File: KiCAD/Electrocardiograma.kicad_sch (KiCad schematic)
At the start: 48 parts, among them J2 Conn_01x02_Pin, J3 AudioJack4, SW1 SW_DPST_x2, U1 INA823DT, U2 ESP32-C3-WROOM-02, U4 TLV4888, U5 TLV4888

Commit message: Es raro mandar cada cambio por si acaso tu lo quieres ver
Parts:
- added U3: AMS1117-3.3, Package_TO_SOT_SMD:SOT-223-3_TabPin2, symbol Regulator_Linear:AMS1117-3.3
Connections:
- net +BATT: now also U3.3 (VI)
- net -BATT: now also U2.19 (GND), U2.9 (GND), U3.1 (GND)
- net +3.3V: now reaches U2.1 (3V3)
- net +3.3V: now also U2.2 (EN), U3.2 (VO)
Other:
- moved on the sheet: U2

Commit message: footprints resistencias
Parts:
- R1, R10, R11, R12, R13, R14, R15, R16, R17, R18, R19, R2, R20, R21, R22, R23, R24, R25, R26, R27, R3, R4, R5, R6, R7, R8, R9: footprint (none) -> Resistor_SMD:R_0805_2012Metric
- SW1: footprint (none) -> Button_Switch_THT:SW_Push_2P1T_Toggle_CK_PVA1xxH1xxxxxxV2
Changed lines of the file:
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@@
 			)
 		)
-		(property "Footprint" ""
+		(property "Footprint" "Resistor_SMD:R_0805_2012Metric"
 			(at 130.81 97.028 90)
 			(hide yes)
@@
 			)
 		)
-		(property "Footprint" ""
+		(property "Footprint" "Resistor_SMD:R_0805_2012Metric"
 			(at 80.01 165.608 90)
 			(hide yes)
@@
 			)
 		)
-		(property "Footprint" ""
+		(property "Footprint" "Resistor_SMD:R_0805_2012Metric"
 			(at 96.012 59.69 90)
 			(hide yes)
@@
 			)
 		)
-		(property "Footprint" ""
+		(property "Footprint" "Resistor_SMD:R_0805_2012Metric"
 			(at 33.02 151.638 90)
 			(hide yes)
@@
 			)
 		)
-		(property "Footprint" ""
+		(property "Footprint" "Resistor_SMD:R_0805_2012Metric"
 			(at 85.852 59.69 90)
 			(hide yes)
@@
 			)
 		)
-		(property "Footprint" ""
+		(property "Footprint" "Resistor_SMD:R_0805_2012Metric"
 			(at 50.038 102.87 90)
 			(hide yes)
@@
 			)
 		)
-		(property "Footprint" ""
+		(property "Footprint" "Button_Switch_THT:SW_Push_2P1T_Toggle_CK_PVA1xxH1xxxxxxV2"
 			(at 261.62 29.21 0)
 			(hide yes)
@@
 			)
 		)
-		(property "Footprint" ""
+		(property "Footprint" "Resistor_SMD:R_0805_2012Metric"
 			(at 85.852 24.13 90)
 			(hide yes)
@@
 			)
 		)
-		(property "Footprint" ""
+		(property "Footprint" "Resistor_SMD:R_0805_2012Metric"
 			(at 133.35 139.192 90)
 			(hide yes)
@@
 			)
 		)
-		(property "Footprint" ""
+		(property "Footprint" "Resistor_SMD:R_0805_2012Metric"
 			(at 116.84 139.192 90)
 			(hide yes)
@@
 			)
 		)
-		(property "Footprint" ""
+		(property "Footprint" "Resistor_SMD:R_0805_2012Metric"
 			(at 68.072 170.18 90)
 			(hide yes)
@@
 			)
 		)
-		(property "Footprint" ""
+		(property "Footprint" "Resistor_SMD:R_0805_2012Metric"
 			(at 85.852 34.29 90)
 			(hide yes)
@@
 			)
 		)
-		(property "Footprint" ""
+		(property "Footprint" "Resistor_SMD:R_0805_2012Metric"
 			(at 96.012 49.53 90)
 			(hide yes)
@@
 			)
 		)
-		(property "Footprint" ""
+		(property "Footprint" "Resistor_SMD:R_0805_2012Metric"
 			(at 51.562 113.03 90)
 			(hide yes)
@@
 			)
 		)
-		(property "Footprint" ""
+		(property "Footprint" "Resistor_SMD:R_0805_2012Metric"
 			(at 41.148 168.91 90)
 			(hide yes)
@@
 			)
 		)
-		(property "Footprint" ""
+		(property "Footprint" "Resistor_SMD:R_0805_2012Metric"
 			(at 85.852 49.53 90)
 			(hide yes)
@@
 			)
 		)
-		(property "Footprint" ""
+		(property "Footprint" "Resistor_SMD:R_0805_2012Metric"
 			(at 46.482 168.91 90)
 			(hide yes)
@@
 			)
 		)
-		(property "Footprint" ""
+		(property "Footprint" "Resistor_SMD:R_0805_2012Metric"
 			(at 59.69 107.442 90)
 			(hide yes)
@@
 			)
 		)
-		(property "Footprint" ""
+		(property "Footprint" "Resistor_SMD:R_0805_2012Metric"
 			(at 146.812 156.21 90)
 			(hide yes)
@@
 			)
 		)
-		(property "Footprint" ""
+		(property "Footprint" "Resistor_SMD:R_0805_2012Metric"
 			(at 55.88 64.262 90)
 			(hide yes)
@@
 			)
 		)
-		(property "Footprint" ""
+		(property "Footprint" "Resistor_SMD:R_0805_2012Metric"
 			(at 41.91 89.408 90)
 			(hide yes)
@@
 			)
 		)
-		(property "Footprint" ""
+		(property "Footprint" "Resistor_SMD:R_0805_2012Metric"
 			(at 154.94 150.622 90)
 			(hide yes)
@@
 			)
 		)
-		(property "Footprint" ""
+		(property "Footprint" "Resistor_SMD:R_0805_2012Metric"
 			(at 30.988 44.45 90)
 			(hide yes)
@@
 			)
 		)
-		(property "Footprint" ""
+		(property "Footprint" "Resistor_SMD:R_0805_2012Metric"
 			(at 40.64 64.262 90)
 			(hide yes)
@@
 			)
 		)
-		(property "Footprint" ""
+		(property "Footprint" "Resistor_SMD:R_0805_2012Metric"
 			(at 54.61 151.638 90)
 			(hide yes)
@@
 			)
 		)
-		(property "Footprint" ""
+		(property "Footprint" "Resistor_SMD:R_0805_2012Metric"
 			(at 144.018 59.69 90)
 			(hide yes)
@@
 			)
 		)
-		(property "Footprint" ""
+		(property "Footprint" "Resistor_SMD:R_0805_2012Metric"
 			(at 146.05 86.868 90)
 			(hide yes)
@@
 			)
 		)
-		(property "Footprint" ""
+		(property "Footprint" "Resistor_SMD:R_0805_2012Metric"
 			(at 144.018 49.53 90)
 			(hide yes)

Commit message: Configuración de programación ESP32-C3
añadí las resistencias que se necesitan para establecer el boot

Ademas separé las etapas del esquematico
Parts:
- added J4, J5: Conn_01x02_Pin, symbol Connector:Conn_01x02_Pin
- added R28, R29, R30: 10K, Resistor_SMD:R_0805_2012Metric, symbol Device:R
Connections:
- net +3.3V: now also R28.2, R29.2, R30.2; no longer U2.2 (EN)
- net GND: now also J4.2 (Pin_2), J5.2 (Pin_2)
- net USB_D-: now reaches U2.13 (IO18)
- net USB_D+: now reaches U2.14 (IO19)
- net ADC_3: now reaches U2.15 (IO3)
- net ADC_1: now reaches U2.17 (IO1)
- net ADC_0: now reaches U2.18 (IO0)
- net Boot1: now reaches U2.7 (IO8)
- net Boot1: now also R29.1
- net Boot2: now reaches U2.8 (IO9)
- net Boot2: now also J4.1 (Pin_1), R30.1
- new net Reset: J5.1 (Pin_1), R28.1, U2.2 (EN)
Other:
- note added: "Alimentación"
- note added: "Corto-circuitar para entrar cargar codigo"
- note added: "ESP32-C3"
- note added: "Estas son las entradas Analog to Digital"
- note added: "J: Me gustaria poner led's de este lado para indicar si la carga del codigo está completa o incluso mostrar el pulso del corazon "R""
- note added: "Las entradas USB deben ir protegidas con TVS, pero si solo se ocupan una vez quizas no sea necesario"
- moved on the sheet: C1, C11, C12, C2, C3, C4, C7, D1, J2, R12, R16, R18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

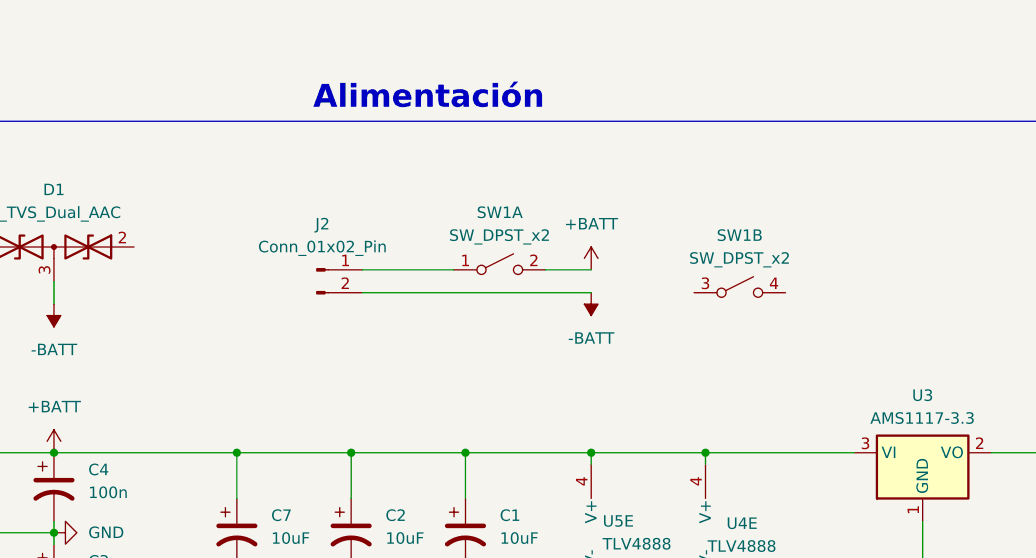
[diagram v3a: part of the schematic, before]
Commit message: Add Voltage Regulator 5V and 1N4007; update schematic
Add Diode 1N4007 for protection and TLV1117-50  for voltage regulation. Apply schematic coordinate, wire and junction adjustments to reflect the updated components and routing.
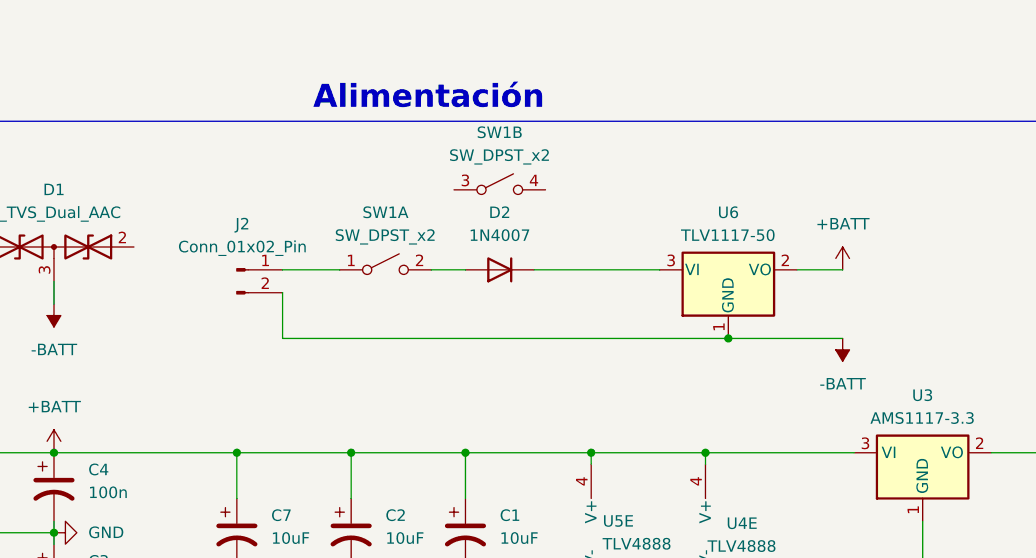
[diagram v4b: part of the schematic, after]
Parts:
- added D2: 1N4007, Diode_THT:D_DO-41_SOD81_P7.62mm_Horizontal, symbol Diode:1N4007
- added U6: TLV1117-50, Package_TO_SOT_SMD:SOT-223-3_TabPin2, symbol Regulator_Linear:TLV1117-50
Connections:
- net +BATT: now also U6.2 (VO); no longer SW1.2 (B)
- net -BATT: now also U6.1 (GND)
- new net: D2.2 (A), SW1.2 (B)
- new net: D2.1 (K), U6.3 (VI)
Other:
- moved on the sheet: J2, SW1A, SW1B

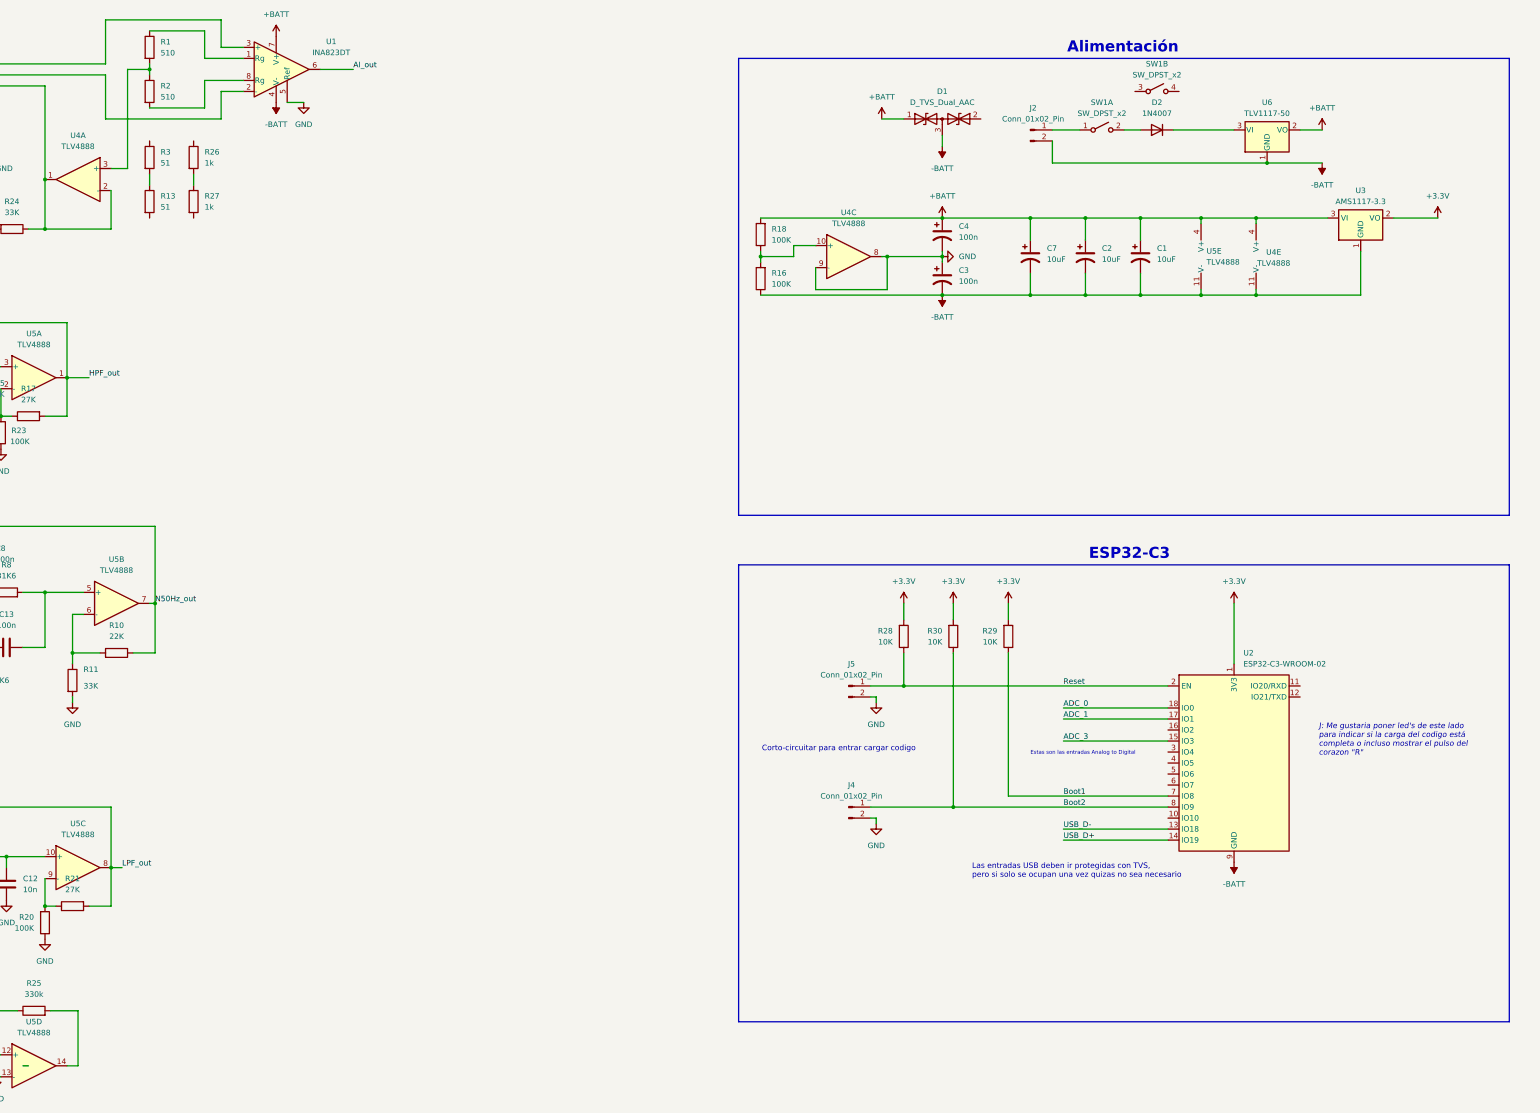
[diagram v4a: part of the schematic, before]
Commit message: Update KiCAD PCB footprints and pad geometry
Replace and correct multiple footprints  across the PCB. Also add/replace a TO-252/SOT regulator footprint for TLV1117-33 with proper pad geometry and net assignments, update DigiKey/Datasheet fields and numerous UUIDs.
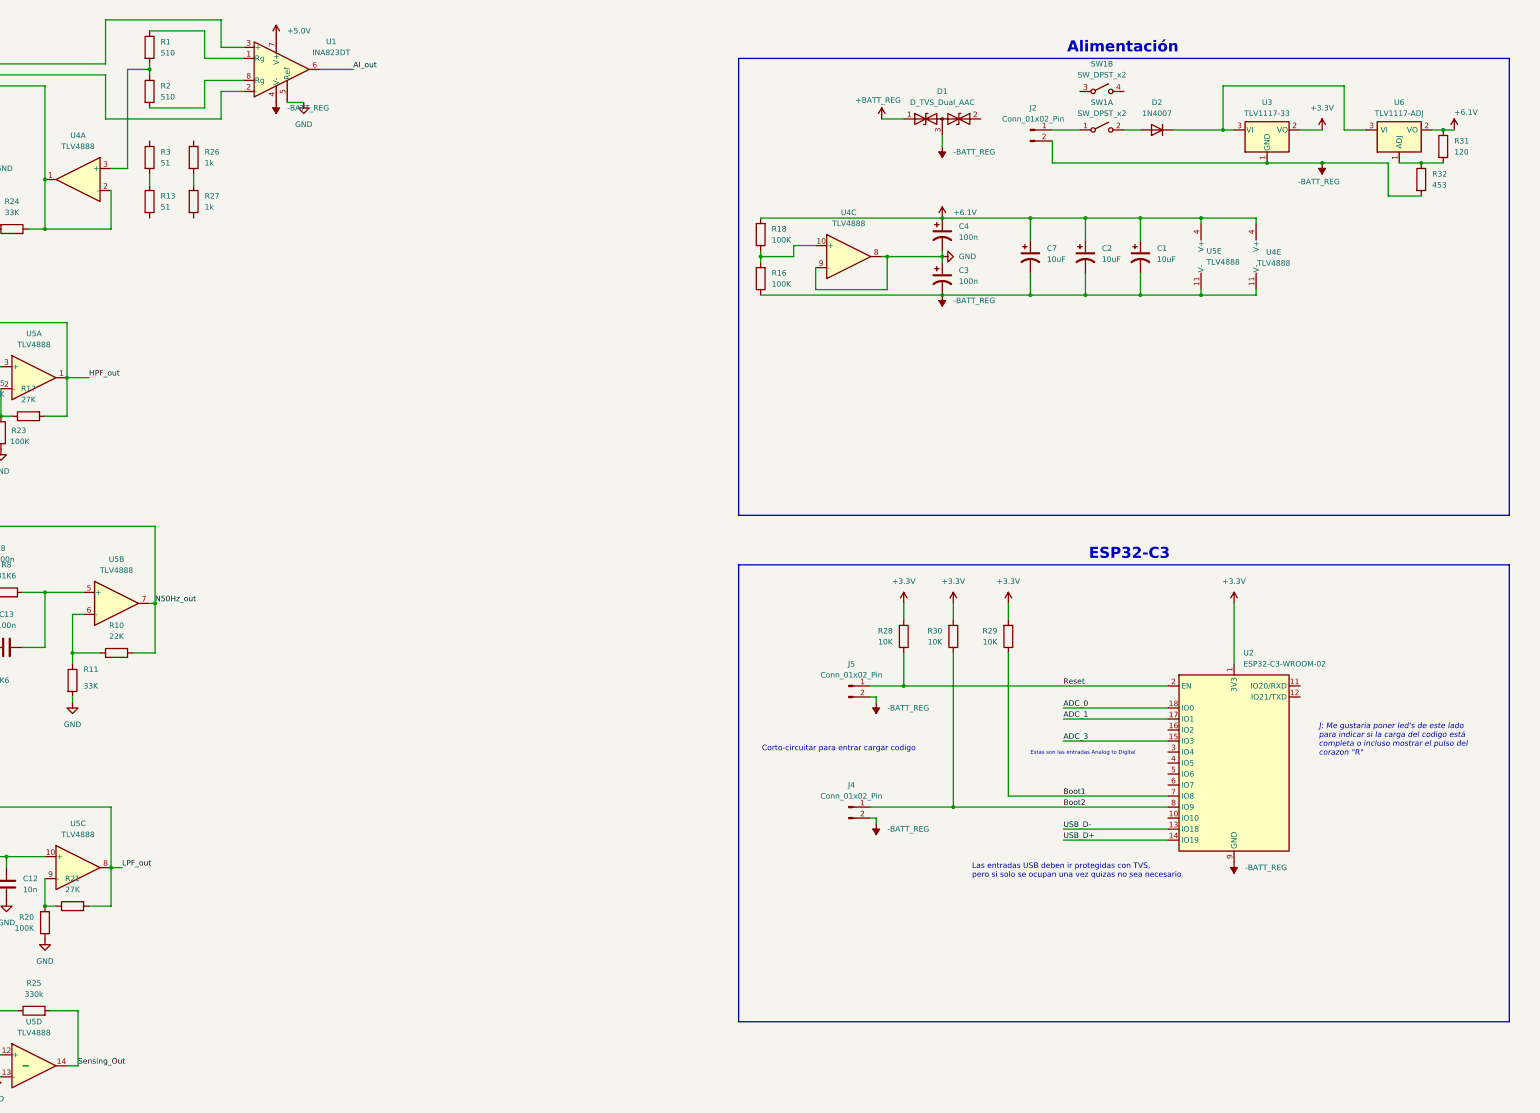
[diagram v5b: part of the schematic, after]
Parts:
- removed U3: AMS1117-3.3, Package_TO_SOT_SMD:SOT-223-3_TabPin2, symbol Regulator_Linear:AMS1117-3.3
- removed U6: TLV1117-50, Package_TO_SOT_SMD:SOT-223-3_TabPin2, symbol Regulator_Linear:TLV1117-50
- added R31: 120, Resistor_SMD:R_0805_2012Metric_Pad1.20x1.40mm_HandSolder, symbol Device:R
- added R32: 453, Resistor_SMD:R_0805_2012Metric_Pad1.20x1.40mm_HandSolder, symbol Device:R
- added U3: TLV1117-33, Package_TO_SOT_SMD:TO-252-2, symbol Regulator_Linear:TLV1117-33
- added U6: TLV1117-ADJ, Package_TO_SOT_SMD:SOT-223-3_TabPin2, symbol Regulator_Linear:TLV1117-ADJ
- C1, C10, C11, C12, C2, C7, C9: footprint (none) -> Capacitor_SMD:C_0805_2012Metric_Pad1.18x1.45mm_HandSolder
- C13, C3, C4, C5, C6, C8: footprint (none) -> Capacitor_SMD:C_1206_3216Metric_Pad1.33x1.80mm_HandSolder
- R1, R10, R11, R12, R13, R14, R15, R16, R17, R18, R19, R2, R20, R21, R22, R23, R24, R25, R26, R27, R28, R29, R3, R30, R4, R5, R6, R7, R8, R9: footprint Resistor_SMD:R_0805_2012Metric -> Resistor_SMD:R_0805_2012Metric_Pad1.20x1.40mm_HandSolder
- U4: footprint (none) -> Package_SO:SOIC-14_3.9x8.7mm_P1.27mm
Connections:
- net +3.3V: now also U3.2 (VO)
- net GND: no longer J4.2 (Pin_2), J5.2 (Pin_2)
- net Sensing_Out: now reaches R25.2, U5.14
- net at D2.1 (K): now also U3.3 (VI), U6.3 (VI)
- net +BATT renamed +6.1V
- net +6.1V: now also R31.1, U6.2 (VO); no longer D1.1 (A1), U1.7 (V+)
- net -BATT renamed -BATT_REG
- net -BATT_REG: now also J4.2 (Pin_2), J5.2 (Pin_2), R32.2, U3.1 (GND)
- new net: R31.2, R32.1, U6.1 (ADJ)
- new net +5.0V: U1.7 (V+)
- new net +BATT_REG: D1.1 (A1)
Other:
- moved on the sheet: SW1B

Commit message: Fixed Diode and Resistors mistaken  Models
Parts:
- D2: footprint Diode_THT:D_DO-41_SOD81_P7.62mm_Horizontal -> Diode_SMD:D_SMA_Handsoldering; DigiKey (none) -> 5399-M7CT-ND
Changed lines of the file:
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@@
 			)
 		)
-		(property "Footprint" "Diode_THT:D_DO-41_SOD81_P7.62mm_Horizontal"
+		(property "Footprint" "Diode_SMD:D_SMA_Handsoldering"
 			(at 320.04 38.735 0)
 			(hide yes)
@@
 			(at 320.04 43.18 0)
 			(hide yes)
+			(show_name no)
+			(do_not_autoplace no)
+			(effects
+				(font
+					(size 1.27 1.27)
+				)
+			)
+		)
+		(property "DigiKey" "5399-M7CT-ND"
+			(at 320.04 43.18 0)
+			(hide yes)

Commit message: Corte de placa y plano de tierra en botton y top layer
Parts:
- D1: footprint Diode_SMD:D_SOD-323_HandSoldering -> Package_TO_SOT_SMD:SOT-23
- J2, J4, J5: footprint (none) -> Connector_JST:JST_XH_B2B-XH-AM_1x02_P2.50mm_Vertical
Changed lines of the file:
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@@
 			)
 		)
-		(property "Footprint" "Diode_SMD:D_SOD-323_HandSoldering"
+		(property "Footprint" "Package_TO_SOT_SMD:SOT-23"
 			(at 266.7 40.64 0)
 			(hide yes)
@@
 			)
 		)
-		(property "Footprint" ""
+		(property "Footprint" "Connector_JST:JST_XH_B2B-XH-AM_1x02_P2.50mm_Vertical"
 			(at 290.83 43.18 0)
 			(hide yes)
@@
 			)
 		)
-		(property "Footprint" ""
+		(property "Footprint" "Connector_JST:JST_XH_B2B-XH-AM_1x02_P2.50mm_Vertical"
 			(at 248.92 171.45 0)
 			(hide yes)
@@
 			)
 		)
-		(property "Footprint" ""
+		(property "Footprint" "Connector_JST:JST_XH_B2B-XH-AM_1x02_P2.50mm_Vertical"
 			(at 248.92 199.39 0)
 			(hide yes)

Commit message: .
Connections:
- net +5.0V is gone; now on net +6.1V: U1.7 (V+)
- net +BATT_REG is gone; now on net +BATT: D1.1 (A1)
- net +BATT: now reaches D2.2 (A), SW1.2 (B)
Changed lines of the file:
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@@
 		(title "Modulo Sensado ECG")
 		(date "2026-06-05")
-		(rev "0005")
+		(rev "0006")
 		(company "Escobar-Ortega")
 	)
@@
 	)
 	(junction
+		(at 316.23 43.18)
+		(diameter 0)
+		(color 0 0 0 0)
+	)
+	(junction
 		(at 39.37 165.1)
 		(diameter 0)
@@
 	)
 	(symbol
+		(lib_id "power:+BATT")
+		(at 316.23 43.18 0)
+		(unit 1)
+		(body_style 1)
+		(exclude_from_sim no)
+		(in_bom yes)
+		(on_board yes)
+		(in_pos_files yes)
+		(dnp no)
+		(property "Reference" "#PWR023"
+			(at 316.23 46.99 0)
+			(hide yes)
+			(show_name no)
+			(do_not_autoplace no)
+			(effects
+				(font
+					(size 1.27 1.27)
+				)
+			)
+		)
+		(property "Value" "+BATT"
+			(at 310.134 38.862 0)
+			(show_name no)
+			(do_not_autoplace no)
+			(effects
+				(font
+					(size 1.27 1.27)
+				)
+				(justify left)
+			)
+		)
+		(property "Footprint" ""
+			(at 316.23 43.18 0)
+			(hide yes)
+			(show_name no)
+			(do_not_autoplace no)
+			(effects
+				(font
+					(size 1.27 1.27)
+				)
+			)
+		)
+		(property "Datasheet" ""
+			(at 316.23 43.18 0)
+			(hide yes)
+			(show_name no)
+			(do_not_autoplace no)
+			(effects
+				(font
+					(size 1.27 1.27)
+				)
+			)
+		)
+		(property "Description" "Power symbol creates a global label with name \"+BATT\""
+			(at 316.23 43.18 0)
+			(hide yes)
+			(show_name no)
+			(do_not_autoplace no)
+			(effects
+				(font
+					(size 1.27 1.27)
+				)
+			)
+		)
+		(pin "1"
+		)
+		(instances
+			(project "Electrocardiograma"
+				(path "/daa88958-acc8-459e-83b6-465edaf551be"
+					(reference "#PWR023")
+					(unit 1)
+				)
+			)
+		)
+	)
+	(symbol
 		(lib_name "R_2")
 		(lib_id "Device:R")
@@
 			)
 		)
-		(property "Value" "+5.0V"
+		(property "Value" "+6.1V"
 			(at 119.38 20.3199 0)
 			(show_name no)
@@
 			)
 		)
-		(property "Value" "+BATT_REG"
+		(property "Value" "+BATT"
 			(at 250.444 36.322 0)
 			(show_name no)
